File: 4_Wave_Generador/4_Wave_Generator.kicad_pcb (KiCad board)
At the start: 2 copper layers, 100 x 100 mm, 121 parts, among them J1 RS232, J10 Jumper, J11 Jumper, J12 Jumper, J13 Jumper, J14 Jumper, J15 Jumper, J2 I2C, J3 RS232_PIC, J4 RESET, J5 Jumper, J7 Jumper, P1 ECG INPUTS, P10 INPUT_ADC_PIC, P11 IN_MUX1, P12 RG_8421, P13 IN_MUX2, P14 OUTPUT_TARJET, P15 OUTPUT_DIG_PIC, P16 OUTPUT_DIG_ATMEGA328P, P17 SUPPLY_-12V, P2 PIC_PROGRAMER, P3 SPI_MICRO, P4 AD8232_CONTROL, P5 OXIMETRO, P6 SUPPLY_12V, P7 SUPPLY_VDD, P8 MCLK_EXTERNAL, P9 SPI_AD9833, SW1 SW_Push, SW2 RESET_PIC, U1 PIC16F688, U2 AD8232_A, U3 ATMEGA328P-AU_MIO, U4 AD9833, U5 LD1117S33TR_MIO, U6 ADG819, U7 ADG819, U8 AD8421, Y1 Crystal_8MHz, Y2 XRCHA_16M

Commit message: GENERADOR_V9
DISTRIBUCION DE COMPONENTES
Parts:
- removed C13: 0.1uF, Capacitors_SMD:C_0805_HandSoldering
- removed J1: RS232, Foot_Prints_Manager_Outputs:RS232
- removed J2: I2C, Foot_Prints_Manager_Outputs:I2C_2X4
- removed J3: RS232_PIC, Foot_Prints_Manager_Outputs:RS232
- removed P11: IN_MUX1, Foot_Prints_Manager_Outputs:IN_MUX1
- added C9: 0.1uF, Capacitors_SMD:C_0805_HandSoldering, F.Cu at (120.0, 94.9)
- added J6: Jumper, Pin_Headers:Pin_Header_Straight_1x02_Pitch2.54mm, F.Cu at (120.3, 87.8)
- added J8: Jumper, Pin_Headers:Pin_Header_Straight_1x02_Pitch2.54mm, F.Cu at (133.0, 100.0)
- added JP6: MIN_SANGRADO, Pin_Headers:Pin_Header_Straight_1x03_Pitch2.54mm, F.Cu at (131.8, 106.8)
- added P18: RS232, Foot_Prints_Manager_Outputs:RS232, F.Cu at (129.2, 41.8)
- added P19: I2C, Foot_Prints_Manager_Outputs:I2C_2X4, F.Cu at (154.7, 41.6)
- added P20: PD6, Pin_Headers:Pin_Header_Straight_1x01_Pitch2.54mm, F.Cu at (137.2, 85.3)
- added P21: PD7, Pin_Headers:Pin_Header_Straight_1x01_Pitch2.54mm, F.Cu at (141.0, 85.3)
- added P22: PB0, Pin_Headers:Pin_Header_Straight_1x01_Pitch2.54mm, F.Cu at (144.9, 85.3)
- added P23: PB1, Pin_Headers:Pin_Header_Straight_1x01_Pitch2.54mm, F.Cu at (148.9, 85.3)
- added P24: PC0, Pin_Headers:Pin_Header_Straight_1x01_Pitch2.54mm, F.Cu at (167.3, 74.9)
- added P25: PC1, Pin_Headers:Pin_Header_Straight_1x01_Pitch2.54mm, F.Cu at (167.3, 70.4)
- added P26: PC2, Pin_Headers:Pin_Header_Straight_1x01_Pitch2.54mm, F.Cu at (167.3, 66.1)
- added P27: PC3, Pin_Headers:Pin_Header_Straight_1x01_Pitch2.54mm, F.Cu at (167.2, 61.7)
- added P28: PD2, Pin_Headers:Pin_Header_Straight_1x01_Pitch2.54mm, F.Cu at (128.0, 64.8)
- added P29: PD3, Pin_Headers:Pin_Header_Straight_1x01_Pitch2.54mm, F.Cu at (128.0, 68.6)
- added P30: PD4, Pin_Headers:Pin_Header_Straight_1x01_Pitch2.54mm, F.Cu at (128.0, 72.3)
- added P31: TORNILLO, Mounting_Holes:MountingHole_3.2mm_M3_Pad_Via, F.Cu at (79.2, 43.0)
- added P32: TORNILLO, Mounting_Holes:MountingHole_3.2mm_M3_Pad_Via, F.Cu at (169.2, 43.0)
- added P33: TORNILLO, Mounting_Holes:MountingHole_3.2mm_M3_Pad_Via, F.Cu at (169.2, 133.0)
- added P34: TORNILLO, Mounting_Holes:MountingHole_3.2mm_M3_Pad_Via, F.Cu at (79.2, 133.0)
- added P35: RS232_PIC, Foot_Prints_Manager_Outputs:RS232, F.Cu at (171.0, 110.9)
- added U9: ADG819, Housings_SSOP:MSOP-8_3x3mm_Pitch0.65mm, F.Cu at (123.0, 95.0)
- P13: value IN_MUX2 -> OUTPUT_DIG_PIC; footprint Foot_Prints_Manager_Outputs:IN_MUX2 -> Pin_Headers:Pin_Header_Straight_1x02_Pitch2.54mm
- P15: value OUTPUT_DIG_PIC -> MUX_S1; footprint Pin_Headers:Pin_Header_Straight_1x04_Pitch2.54mm -> Pin_Headers:Pin_Header_Straight_1x02_Pitch2.54mm
- P16: value OUTPUT_DIG_ATMEGA328P -> PD5; footprint Foot_Prints_Manager_Outputs:OUTPUT_ATMEGA -> Pin_Headers:Pin_Header_Straight_1x01_Pitch2.54mm
- moved R21 321.1 mm to (103.2, 57.2)
- moved C25 320.3 mm to (103.2, 65.4), turned to 180 degrees
- moved R24 317.3 mm to (90.9, 42.0)
- moved C32 315.3 mm to (109.8, 69.6), turned to 180 degrees
- moved D5 312.8 mm to (91.3, 46.2)
- moved C33 310.3 mm to (108.3, 76.5)
- moved R18 306.3 mm to (109.6, 102.0), turned to 90 degrees
- moved U4 305.9 mm to (105.3, 72.0), turned to 270 degrees
- moved R19 304.0 mm to (100.9, 102.3), turned to 90 degrees
- moved JP3 301.6 mm to (87.2, 97.5)
- moved C15 301.0 mm to (91.9, 86.9)
- moved C20 299.6 mm to (95.9, 56.0)
- moved C29 298.9 mm to (126.5, 81.6), turned to 180 degrees
- moved J10 297.4 mm to (99.9, 74.4), turned to 270 degrees
- moved C17 286.7 mm to (133.7, 74.9), turned to 180 degrees
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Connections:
- P10 pad 2: /ADC_2 -> /OXIMETRO
- P13 pad 1: /MIN_SANGRADO -> /GND
- P13 pad 2: /GND -> /RC3_PIC
- P15 pad 1: /GND -> /MUX_1_S1
- P15 pad 2: /RC1_PIC -> /MUX_2_S1
- P16 pad 1: /PB1 -> /PWM_ATMEGA
- P5 pad 2: /OXIMETRO -> Net-(P5-Pad2)
- U1 pad 10: /ADC_2 -> /ADC_1
- U1 pad 11: /ADC_1 -> /ADC_2
- U3 pad 10: /PD6 -> /MODULATING_WAVE
- U3 pad 11: /PD7 -> /SELECTOR
- U3 pad 9: /PD5 -> /PWM_ATMEGA
- U6 pad 8: /MODULATED_WAVE_1 -> /BASE_WAVE
- U7 pad 6: /MODULATING_WAVE -> /PWM
- U8 pad 4: /MODULATED_WAVE_2 -> /MODULATED
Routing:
- net /MIN_SANGRADO: track 0.00 -> 19.8 mm, vias 0 -> 2
- net /BASE_WAVE: track 0.00 -> 19.5 mm
- net /PWM: track 0.00 -> 18.3 mm, vias 0 -> 1
- net Net-(J15-Pad2): track 0.00 -> 13.0 mm, vias 0 -> 1
- net /MODULATED_WAVE_1: track 0.00 -> 12.9 mm
- net /MUX_2_S1: track 0.00 -> 12.4 mm
- net /MUX_1_S1: track 0.00 -> 12.3 mm
- net /PWM_ATMEGA: track 0.00 -> 11.5 mm
- net /MODULATED_WAVE_2: track 0.00 -> 10.5 mm
- net Net-(J5-Pad2): track 0.00 -> 9.03 mm
- net /VDD: track 0.00 -> 4.67 mm

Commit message: GENERADOR_V10
RUTEADO MICRO
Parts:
- removed P21: PD7, Pin_Headers:Pin_Header_Straight_1x01_Pitch2.54mm
- removed P22: PB0, Pin_Headers:Pin_Header_Straight_1x01_Pitch2.54mm
- removed P23: PB1, Pin_Headers:Pin_Header_Straight_1x01_Pitch2.54mm
- removed P24: PC0, Pin_Headers:Pin_Header_Straight_1x01_Pitch2.54mm
- removed P25: PC1, Pin_Headers:Pin_Header_Straight_1x01_Pitch2.54mm
- removed P26: PC2, Pin_Headers:Pin_Header_Straight_1x01_Pitch2.54mm
- removed P27: PC3, Pin_Headers:Pin_Header_Straight_1x01_Pitch2.54mm
- removed P28: PD2, Pin_Headers:Pin_Header_Straight_1x01_Pitch2.54mm
- removed P29: PD3, Pin_Headers:Pin_Header_Straight_1x01_Pitch2.54mm
- removed P30: PD4, Pin_Headers:Pin_Header_Straight_1x01_Pitch2.54mm
- added P11: DIG_ATMEGA, Pin_Headers:Pin_Header_Straight_1x04_Pitch2.54mm, F.Cu at (168.3, 70.7)
- P16: value PD5 -> DIG_MICRO; footprint Pin_Headers:Pin_Header_Straight_1x01_Pitch2.54mm -> Pin_Headers:Pin_Header_Straight_1x03_Pitch2.54mm
- P20: value PD6 -> DIG_ATMEGA2; footprint Pin_Headers:Pin_Header_Straight_1x01_Pitch2.54mm -> Pin_Headers:Pin_Header_Straight_1x03_Pitch2.54mm
- moved W9 109.2 mm to (119.2, 54.3)
- moved P16 20.5 mm to (130.9, 64.9)
- moved R21 12.1 mm to (96.7, 47.0), turned to 270 degrees
- moved CLK1 9.96 mm to (98.6, 57.4), turned to 270 degrees
- moved C20 9.80 mm to (100.0, 47.1), turned to 90 degrees
- moved J7 8.74 mm to (97.3, 51.7)
- moved C25 7.93 mm to (105.1, 57.7)
- moved P7 7.82 mm to (114.1, 44.4)
- moved C31 7.69 mm to (110.5, 60.2)
- moved C26 7.45 mm to (105.1, 60.2)
- moved J10 7.10 mm to (99.9, 67.3)
- moved J11 7.10 mm to (99.9, 63.3)
- moved C32 6.85 mm to (110.6, 62.8)
- moved P9 6.10 mm to (98.0, 75.1), turned to 90 degrees
- moved U4 4.92 mm to (107.5, 67.6)
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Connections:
- P16 pad 1: /PWM_ATMEGA -> /PD2
- P20 pad 1: /MODULATING_WAVE -> /PD7
- U3 pad 10: /MODULATING_WAVE -> /SELECTOR
- U3 pad 11: /SELECTOR -> /PD7
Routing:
- net /SCL: track 0.00 -> 44.2 mm
- net /SDA: track 0.00 -> 40.6 mm
- net /Tx: track 0.00 -> 35.2 mm
- net /Rx: track 0.00 -> 34.4 mm
- net /PC3: track 0.00 -> 28.8 mm
- net /SS: track 0.00 -> 28.3 mm
- net /SELECTOR: track 0.00 -> 26.8 mm
- net /MOSI: track 0.00 -> 26.4 mm
- net /PC2: track 0.00 -> 26.3 mm
- net /MISO: track 0.00 -> 25.1 mm
- net /VDD: track 4.67 -> 28.8 mm
- net /PC1: track 0.00 -> 23.5 mm
- net /SCK: track 0.00 -> 23.0 mm
- net /PC0: track 0.00 -> 22.8 mm
- net /RESET: track 0.00 -> 17.5 mm
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
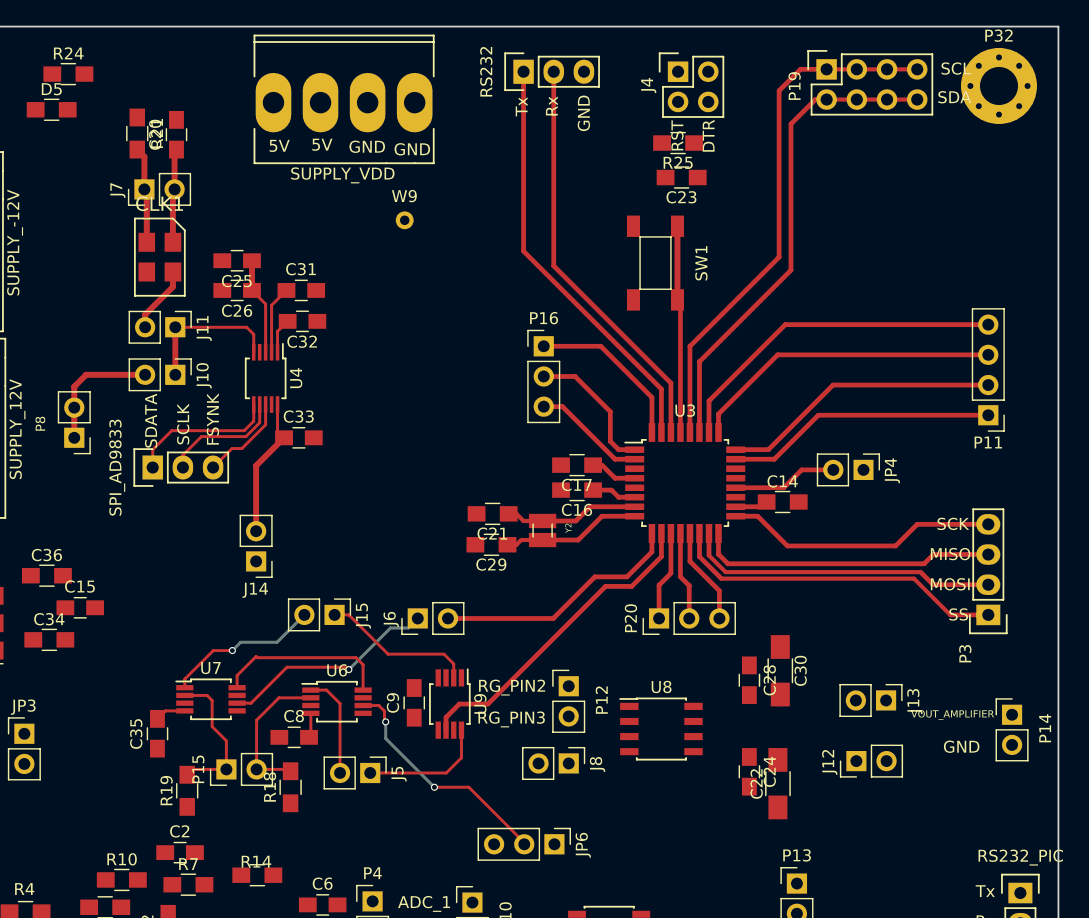
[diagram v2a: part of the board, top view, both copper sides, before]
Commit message: GENERADOR_V11
NUEVAS CONEXIONES
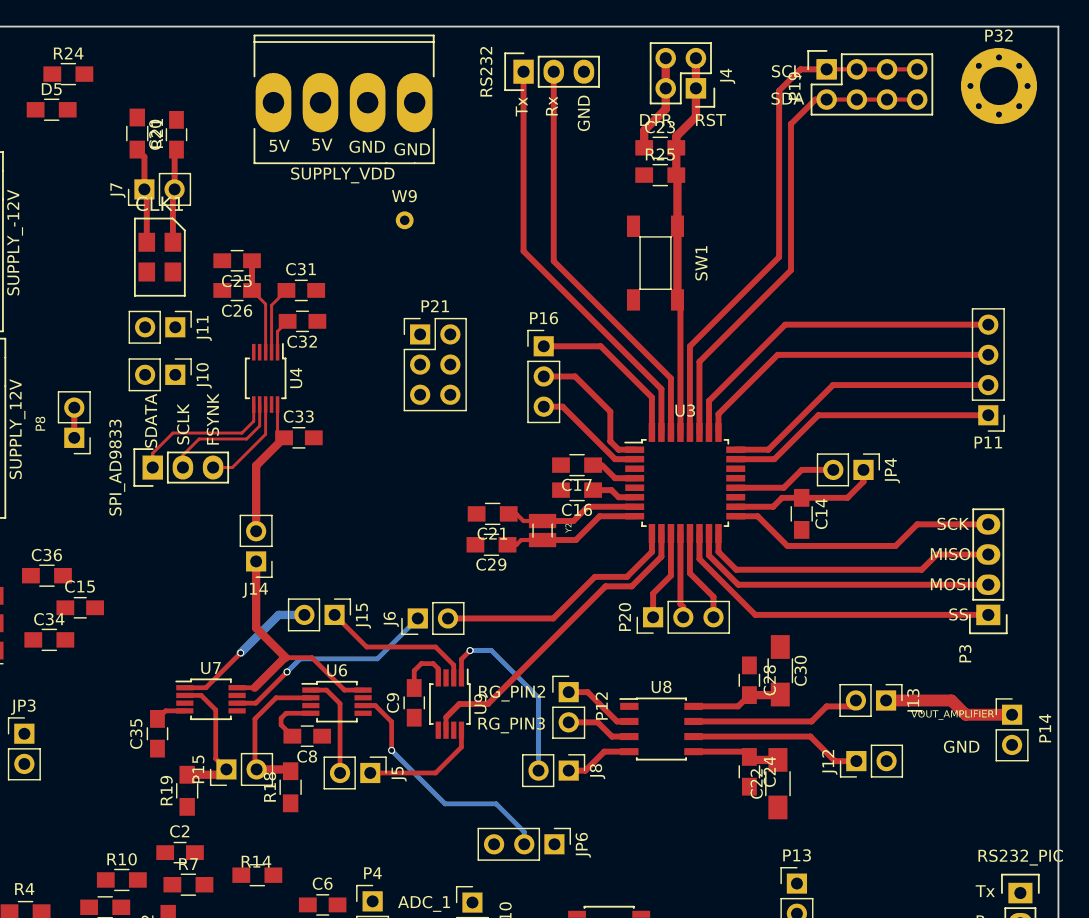
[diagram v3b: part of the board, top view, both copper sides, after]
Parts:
- added P21: CONN_02X03, Pin_Headers:Pin_Header_Straight_2x03_Pitch2.54mm, F.Cu at (120.5, 63.9)
- moved R25 3.09 mm to (140.7, 50.5), turned to 0 degrees
- moved C23 3.08 mm to (140.7, 48.2), turned to 0 degrees
- moved J4 2.05 mm to (143.7, 43.2), turned to 180 degrees
- moved C14 1.89 mm to (152.6, 79.0), turned to 270 degrees
- moved C8 1.10 mm to (111.0, 97.7), turned to 180 degrees
- moved J8 0.60 mm to (133.0, 100.6)
- moved P20 0.51 mm to (140.1, 87.7)
- moved P12 0.50 mm to (133.0, 94.0)
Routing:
- net /VDD: track 28.8 -> 46.7 mm
- net Net-(J8-Pad2): track 0.00 -> 16.1 mm, vias 0 -> 1
- net /RESET: track 17.5 -> 32.7 mm
- net Net-(J12-Pad1): track 0.00 -> 14.6 mm
- net Net-(J13-Pad2): track 0.00 -> 14.4 mm
- net Net-(J10-Pad1): track 12.3 -> 0.00 mm
- net /VOUT_AMPLIFIER: track 0.00 -> 11.1 mm
- net /DTR: track 0.00 -> 8.29 mm
- net Net-(J10-Pad2): track 10.7 -> 2.54 mm
- net /+12V: track 0.00 -> 7.71 mm
- net Net-(J5-Pad2): track 9.03 -> 16.5 mm
- net /-12V: track 0.00 -> 7.39 mm
- net /BASE_WAVE: track 14.7 -> 21.9 mm
- net /RG_PIN2: track 0.00 -> 6.12 mm
- net /MODULATED: track 0.00 -> 5.76 mm
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
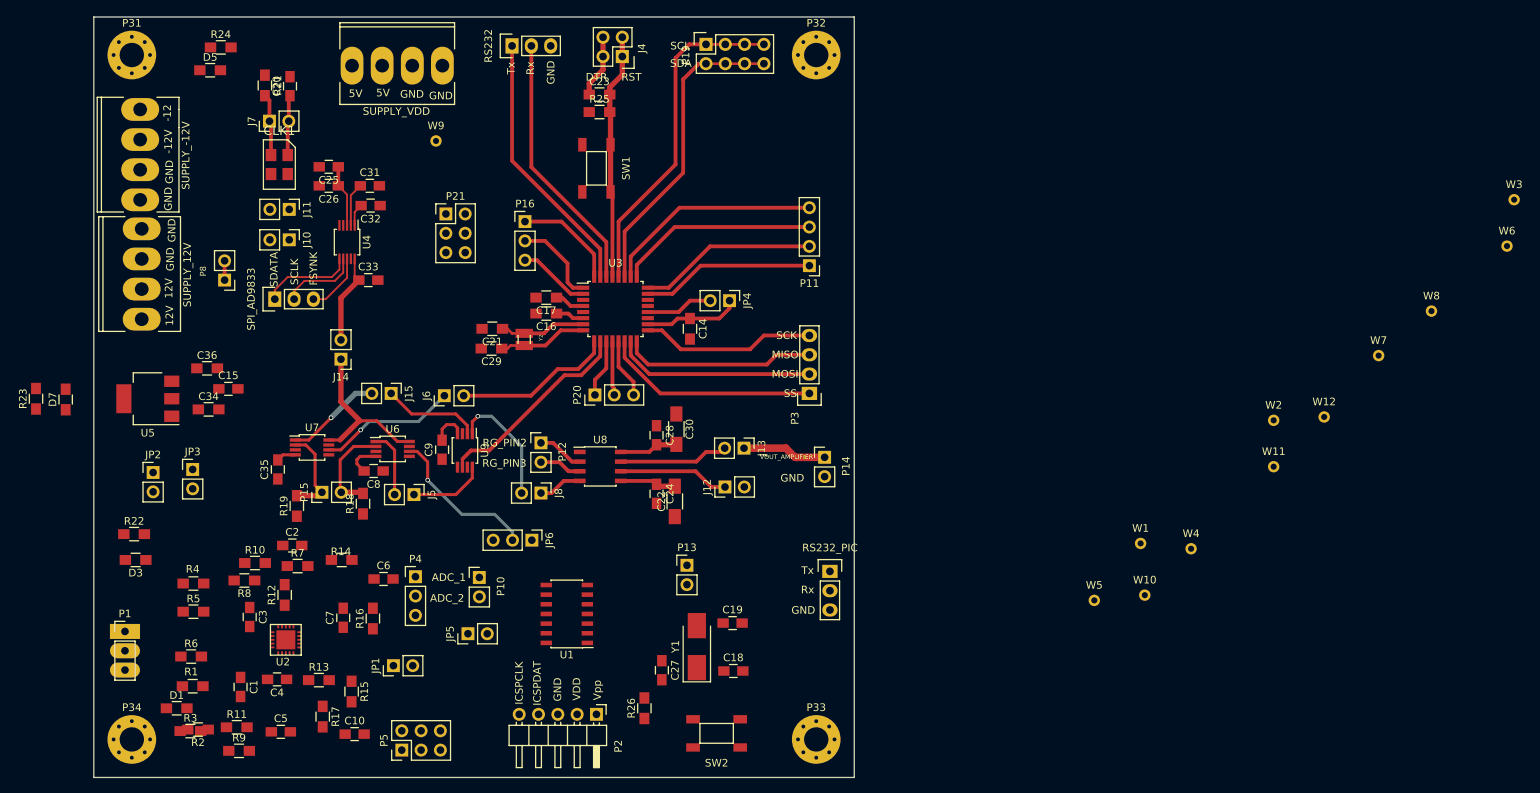
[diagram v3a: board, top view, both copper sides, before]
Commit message: GENERADOR V11
TRAZADO DE PISTAS Y VIAS
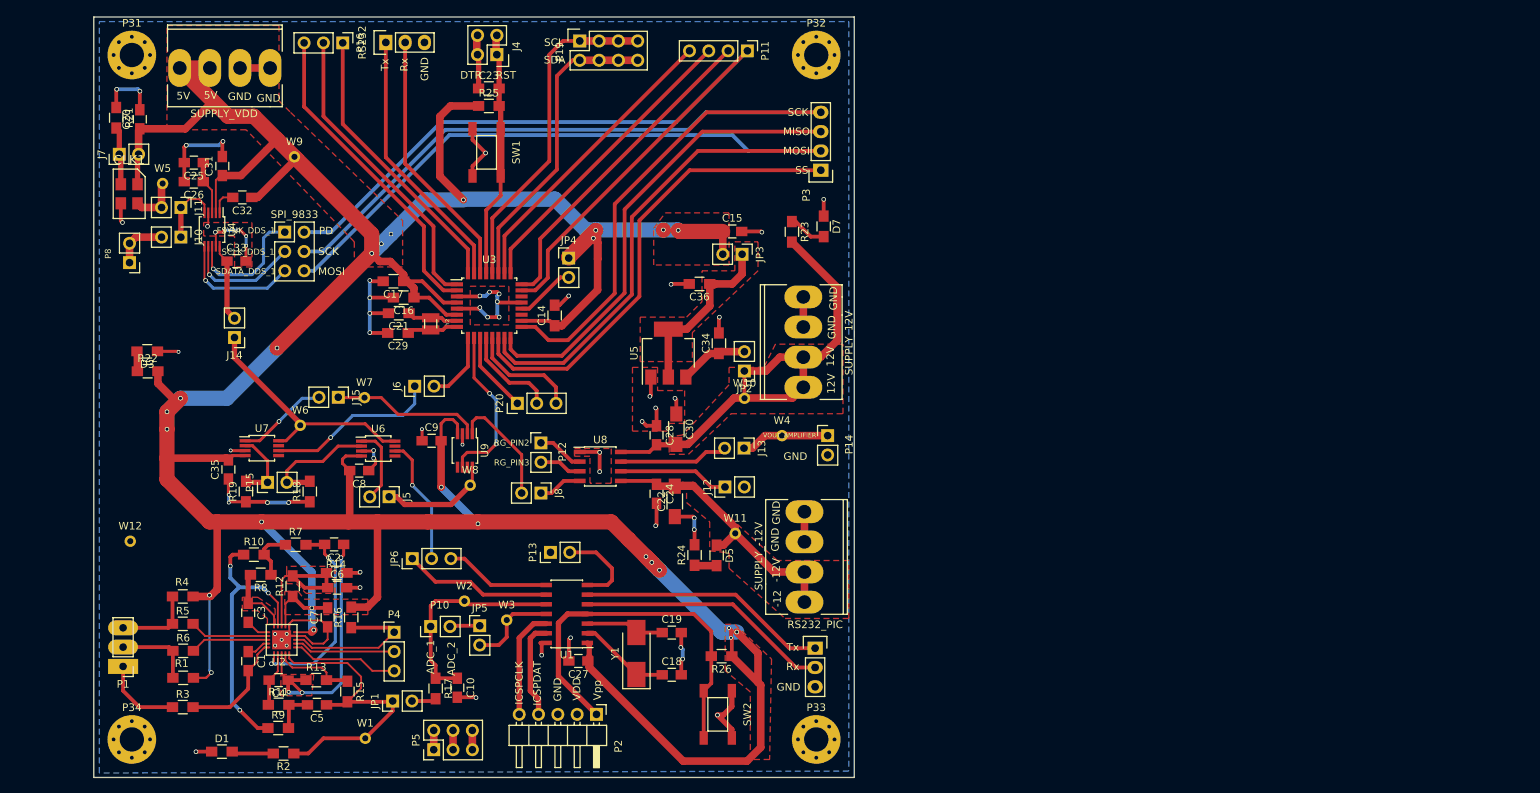
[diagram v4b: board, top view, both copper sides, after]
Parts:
- removed P21: CONN_02X03, Pin_Headers:Pin_Header_Straight_2x03_Pitch2.54mm
- removed P9: SPI_AD9833, Foot_Prints_Manager_Outputs:SPI_AD9833
- added G***: LOGO, Logos_Fuentes:CMOS, B.Cu at (158.2, 129.0)
- added SPI_9833: CONN_02X03, Foot_Prints_Manager_Outputs:SPI_9833, F.Cu at (99.3, 66.3)
- U5: footprint TO_SOT_Packages_SMD:SOT-223 -> Foot_Prints_Manager_Outputs:SOT-223_este
- moved W6 160.4 mm to (101.3, 91.7)
- moved W12 157.8 mm to (79.0, 106.9)
- moved W3 143.5 mm to (128.5, 117.3)
- moved W5 134.2 mm to (83.2, 59.9)
- moved W7 133.5 mm to (109.8, 88.0)
- moved W8 128.5 mm to (123.7, 99.6)
- moved W2 109.0 mm to (122.9, 114.8)
- moved W1 105.1 mm to (109.9, 132.8)
- moved D7 102.2 mm to (170.2, 65.5), turned to 270 degrees
- moved P17 102.1 mm to (167.7, 109.0), turned to 270 degrees
- moved R23 101.8 mm to (166.0, 66.2), turned to 270 degrees
- moved D5 92.2 mm to (156.1, 108.8), turned to 270 degrees
- moved R24 91.3 mm to (153.2, 108.8), turned to 90 degrees
- moved P6 87.5 mm to (167.5, 80.8)
- moved JP2 78.9 mm to (159.8, 84.5), turned to 180 degrees
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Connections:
- P2 pad 2: /VDD -> (no net)
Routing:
- net /VDD: track 46.7 -> 523.6 mm, vias 0 -> 25
- net /GND: track 0.00 -> 206.7 mm, vias 0 -> 61
- net /SCK: track 23.0 -> 134.9 mm
- net /MOSI: track 26.4 -> 137.8 mm
- net /PC0: track 22.8 -> 113.0 mm
- net /+12V: track 7.71 -> 64.3 mm
- net /MCLR/Vpp: track 0.00 -> 50.0 mm
- net /OUT_ANALOG: track 0.00 -> 40.7 mm
- net /IAOUT: track 0.00 -> 37.6 mm, vias 0 -> 3
- net /REFOUT: track 0.00 -> 36.3 mm, vias 0 -> 3
- net /MISO: track 25.4 -> 61.3 mm
- net /SS: track 28.4 -> 62.0 mm
- net /RX_PIC: track 0.00 -> 33.4 mm
- net /-12V: track 7.39 -> 40.6 mm
- net /TX_PIC: track 0.00 -> 32.9 mm
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- added copper zone on F.Cu, net /+12V
- added copper zone on F.Cu, net /-12V
- added copper zone on B.Cu, net /GND
- added copper zone on F.Cu, net /GND
- added copper zone on F.Cu, net /REFIN
- added copper zone on F.Cu, net /REFOUT
- added copper zone on F.Cu, net /VDD
- added copper zone on F.Cu, net Net-(C3-Pad1)
- added copper zone on F.Cu, net Net-(C36-Pad1)

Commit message: GENERADOR_V12
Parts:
- removed C21, C29: 8pF, Resistors_SMD:R_0805_HandSoldering
- removed G***: LOGO, Logos_Fuentes:CMOS
- added C11: 8pF, Resistors_SMD:R_0402, F.Cu at (115.4, 77.6)
- added C12: 8pF, Resistors_SMD:R_0402, F.Cu at (115.3, 79.1)
- moved C36 7.45 mm to (161.2, 71.8), turned to 0 degrees
- moved C34 3.28 mm to (156.1, 84.2), turned to 270 degrees
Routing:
- net Net-(C36-Pad1): track 24.1 -> 9.01 mm
- net /GND: track 206.7 -> 220.4 mm, vias 61 -> 62
- net /VDD: track 523.6 -> 532.6 mm, vias 25 -> 28
- net Net-(C34-Pad1): track 9.08 -> 10.0 mm
- added copper zone on F.Cu, net Net-(C34-Pad1)

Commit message: GENERADOR V13
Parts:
- added G***: LOGO, Logos_Fuentes:Colombia, F.Cu at (80.5, 99.2)
- added G***: LOGO, Logos_Fuentes:SBS_22mm, F.Cu at (146.0, 59.8)
- added G***: LOGO, Logos_Fuentes:UIS, F.Cu at (84.3, 111.2)
- added G***: LOGO, Logos_Fuentes:CMOS, F.Cu at (126.4, 65.5)
- moved W4 0.60 mm to (164.6, 92.5)
- renumbered W11 to -12, U2 to AD8232, U8 to AD8421, U6 to ADG818, U7 to ADG818, U9 to ADG818, W6 to BASE_WAVE, W1 to ECG, W12 to GND, P8 to MCLK_EXT, W7 to MODULATED, W8 to MODULATED, W9 to VDD
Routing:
- net /GND: track 220.4 -> 927.9 mm, vias 62 -> 349
- net /VDD: track 532.6 -> 591.8 mm, vias 28 -> 30
- net /VOUT_AMPLIFIER: track 11.7 -> 24.7 mm
- added copper zone on F.Cu, net Net-(C5-Pad2)
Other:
- board text added: "004 WAVE GENERATOR"
- board text added: "COLOMBIA"
- board text added: "LA"
- board text added: "RA"
- board text added: "RL"
